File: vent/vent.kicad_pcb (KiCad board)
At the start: 2 copper layers, 44.9 x 39.7 mm, 35 parts, among them J1 Valve Control, J2 CAN Connector, J3 Programming Header, J4 Valve Connection, Q1 Q_NMOS_GDS, U1 INA180, U2 MCP2562, U3 PIC18F26K83, Y1 Crystal

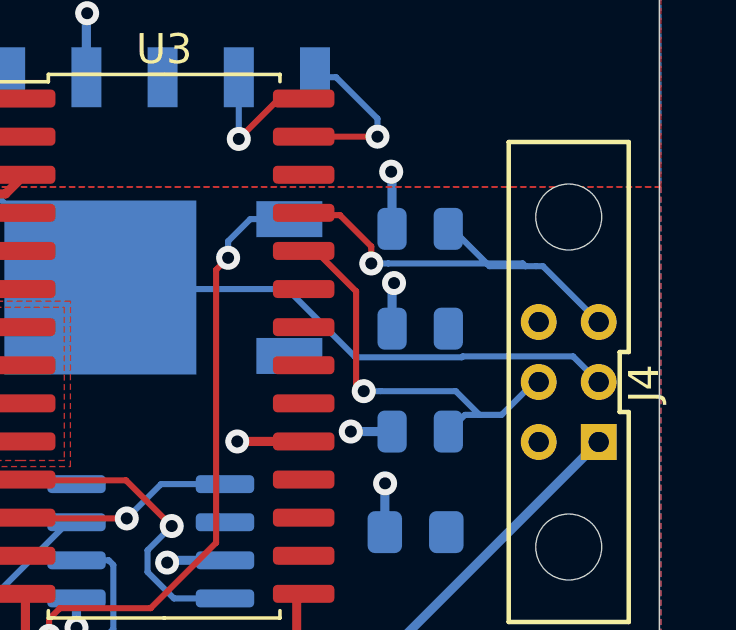
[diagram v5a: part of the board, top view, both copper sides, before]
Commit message: Add board name, fix ground pour islands
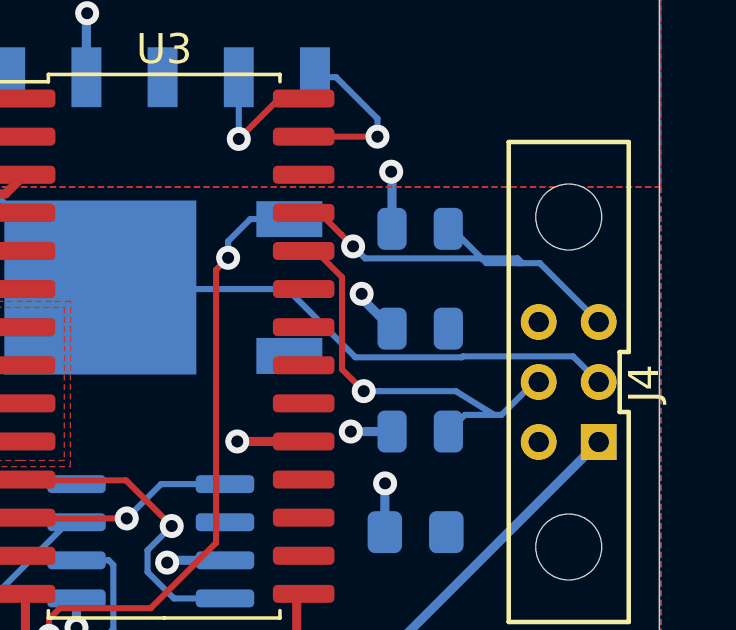
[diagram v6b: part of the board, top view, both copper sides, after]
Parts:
- added G***: LOGO, team_logo:Logo_SilkScreen_10mm, B.Cu at (111.9, 117.2)
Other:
- board text added: "3V3 ~MCLR"
- board text added: "Vent V2 - Baka Jared Watson Matti Gencher 2020-02-20"

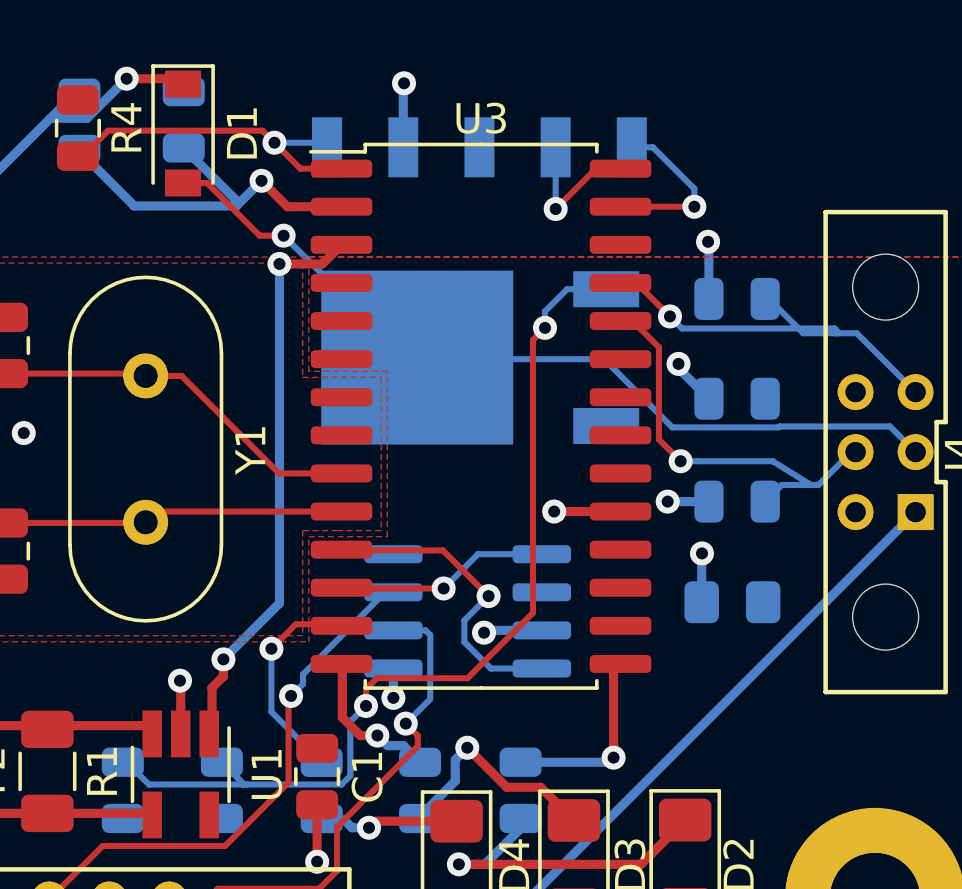
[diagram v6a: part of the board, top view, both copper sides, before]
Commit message: Move MCLR marking, change Q1 footprint to SOT23
I'm fairly certain SOT23 is standard enough for this to be the NMOS we
use. I would like to have a part selected before we advance much further
though.
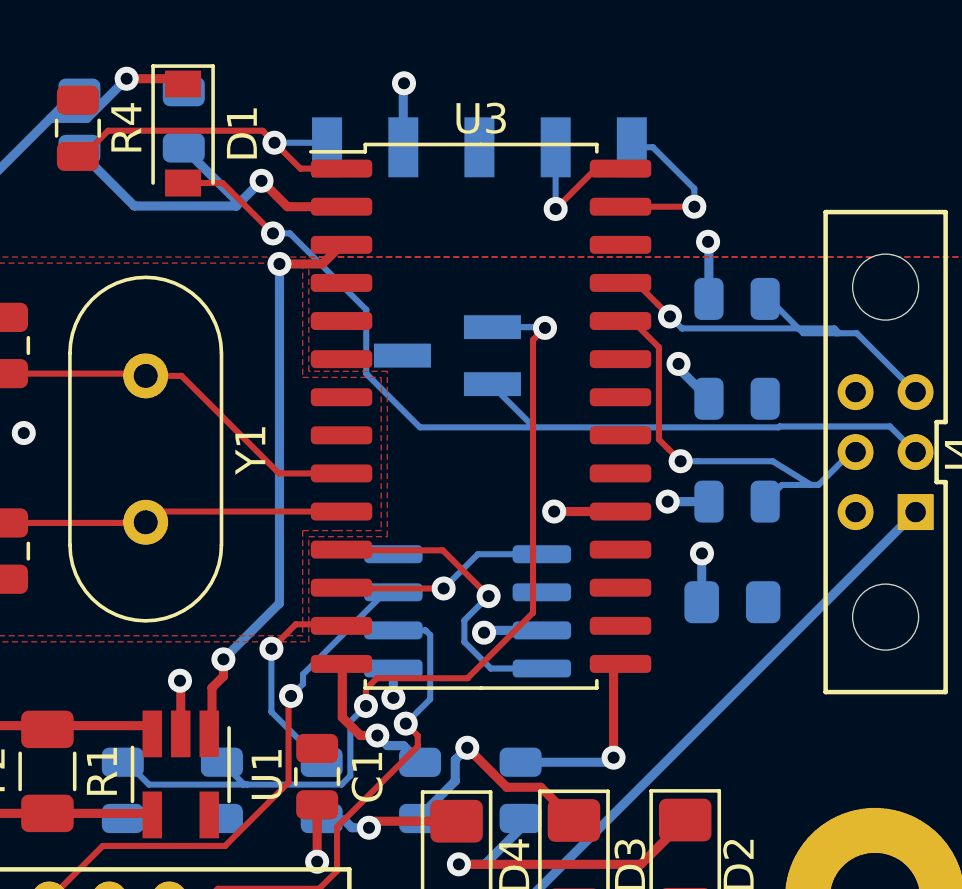
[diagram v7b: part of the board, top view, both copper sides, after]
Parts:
- Q1: footprint Package_TO_SOT_SMD:TO-252-2 -> Package_TO_SOT_SMD:SOT-23_Handsoldering
- moved Q1 1.10 mm to (133.1, 114.0)
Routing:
- net /Valve Control/RELAY-: track 25.8 -> 31.4 mm
- net Net-(Q1-Pad1): track 31.2 -> 30.0 mm

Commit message: Adress Aaron's comments:
- Make Q1 a GSD transistor
- Move D1 next to vent connector
- Move 12V trace away from the edge of the board
- Add LED colour silkscreen
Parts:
- D1: moved to B.Cu
- Q1: value Q_NMOS_GDS -> Q_NMOS_GSD
- moved D1 18.9 mm to (142.4, 111.8), turned to 180 degrees
- moved J1 6.33 mm to (116.0, 104.9)
- moved J3 5.83 mm to (138.1, 112.8)
- moved REF** 5.08 mm to (109.2, 104.1)
- moved REF** 5.08 mm to (147.3, 104.1)
- moved R4 4.86 mm to (125.2, 108.3)
- moved R10 3.85 mm to (142.4, 108.3)
- moved R2 3.60 mm to (122.9, 109.1), turned to 90 degrees
- moved Q1 3.14 mm to (133.9, 117.0)
- moved R3 1.90 mm to (122.9, 104.8)
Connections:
- Q1 pad 2: /Valve Control/RELAY- -> GND
- Q1 pad 3: GND -> /Valve Control/RELAY-
- R8 pad 2: /Valve Control/VALVE_CONTROL -> /MCU/VALVE_CONTROL
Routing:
- net /MCU/VALVE_CONTROL: track 0.00 -> 29.3 mm, vias 0 -> 1
- net +12V: track 89.4 -> 76.2 mm, vias 1 -> 2
- net /Valve Control/RELAY-: track 31.4 -> 22.3 mm, vias 1 -> 0
- net Net-(F1-Pad2): track 19.9 -> 14.1 mm
- net +5V: track 17.0 -> 21.8 mm
- net Net-(D2-Pad1): track 11.0 -> 7.75 mm
- net GND: track 5.90 -> 8.80 mm
- net Net-(Q1-Pad1): track 30.0 -> 27.8 mm
- net /MCU/ICSPDAT: track 4.99 -> 7.00 mm
- net /MCU/CAN_RX: track 10.5 -> 11.9 mm
- net /MCU/~MCLR: track 11.5 -> 10.1 mm
- net /MCU/LIMIT_OPEN: track 14.5 -> 15.7 mm
- net /MCU/LIMIT_CLOSE: track 13.7 -> 12.8 mm
- net /MCU/ICSPCLK: track 5.54 -> 6.41 mm
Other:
- board size 44.9 x 39.7 mm -> 44.9 x 34.6 mm
- board text added: "B"
- board text added: "R"
- board text added: "W"
